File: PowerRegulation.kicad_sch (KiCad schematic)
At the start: 30 parts, among them J11 24V_Lockout_Key_Switch, J12 XT60-M, K1 G5LE-1, Q7 BSS138, U6 XC6206P332MR, U7 TPS5430DDA, U8 TPS5430DDA

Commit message: Fix silk screening
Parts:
- J11, J12, K1: now left out of the parts list
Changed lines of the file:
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@@
 	(title_block
 		(title "Power Distribution")
-		(rev "0.1.0")
+		(rev "1.0.0")
 		(company "Queen's Rocket Engineering Team")
 	)
@@
 		(unit 1)
 		(exclude_from_sim no)
-		(in_bom yes)
+		(in_bom no)
 		(on_board yes)
 		(dnp no)
@@
 		(unit 1)
 		(exclude_from_sim no)
-		(in_bom yes)
+		(in_bom no)
 		(on_board yes)
 		(dnp no)
@@
 		(unit 1)
 		(exclude_from_sim no)
-		(in_bom yes)
+		(in_bom no)
 		(on_board yes)
 		(dnp no)

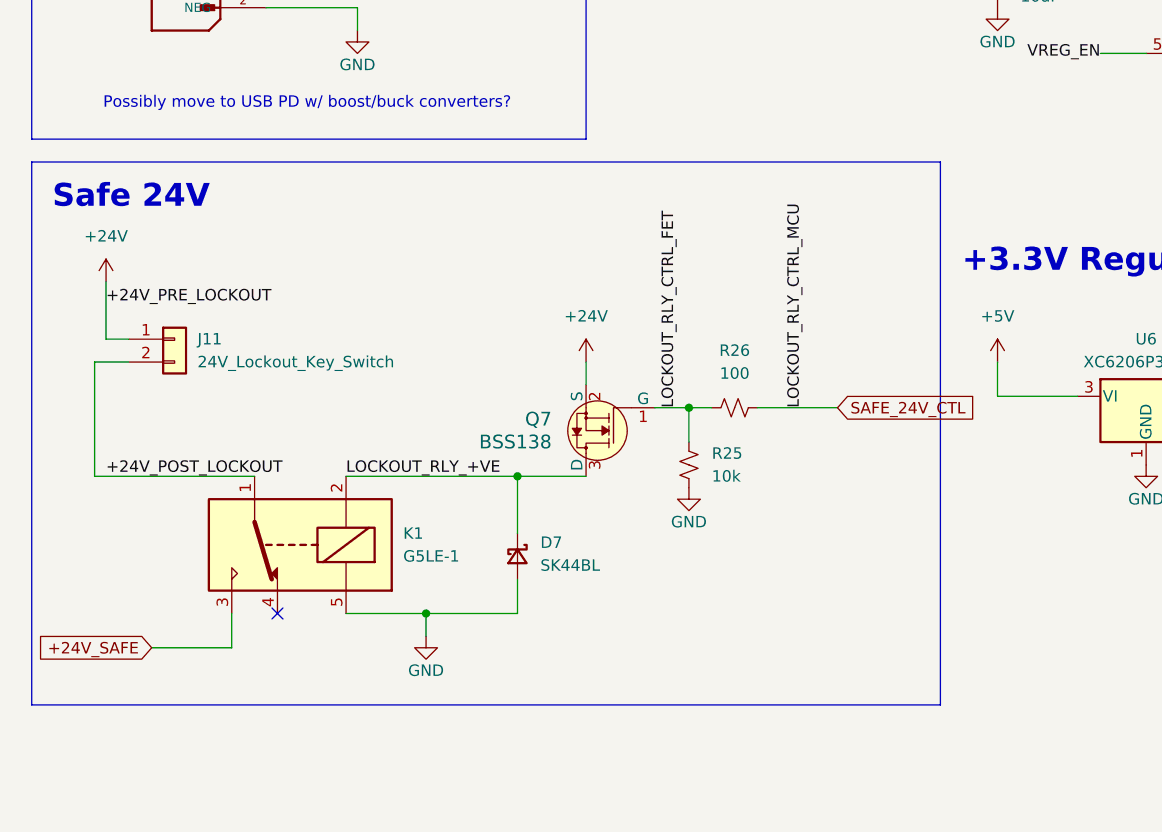
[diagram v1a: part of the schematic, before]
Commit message: Switch relay driving FETs to low side. Relays changed to SPST instead of SPDT
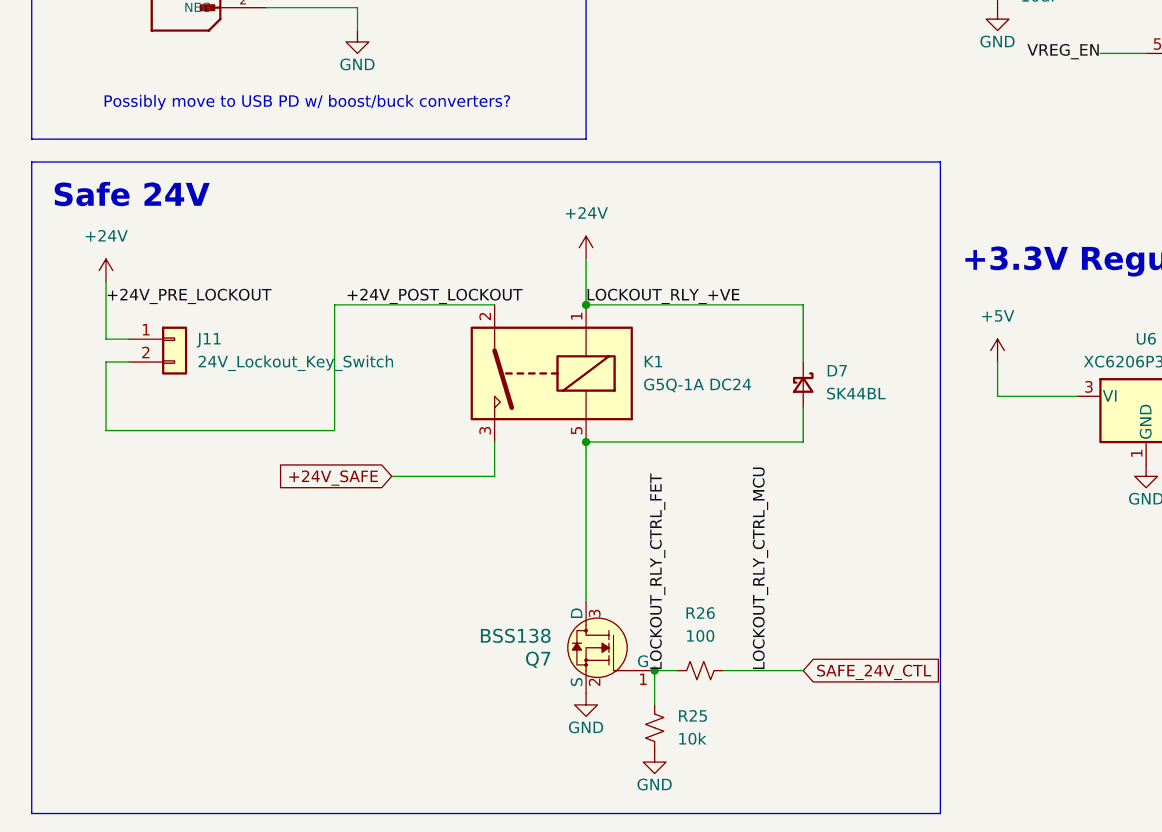
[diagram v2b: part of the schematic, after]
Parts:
- removed K1: G5LE-1, Relay_THT:Relay_SPDT_Omron-G5LE-1, symbol Relay:G5LE-1
- added K1: G5Q-1A DC24, Relay_THT:Relay_SPST_Omron-G5Q-1A, symbol Relay:G5Q-1A
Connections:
- net +24V: now also D7.1 (K), K1.1; no longer Q7.2 (S)
- net +24V_POST_LOCKOUT: now also K1.2
- net +24V_SAFE: now also K1.3
- net GND: now also Q7.2 (S); no longer D7.2 (A)
- net LOCKOUT_RLY_+VE: no longer names the net of Q7.3 (D)
- net LOCKOUT_RLY_+VE: now also D7.2 (A), K1.5; no longer D7.1 (K)
- no-connect marks 2 -> 1
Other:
- moved on the sheet: D7, Q7, R25, R26

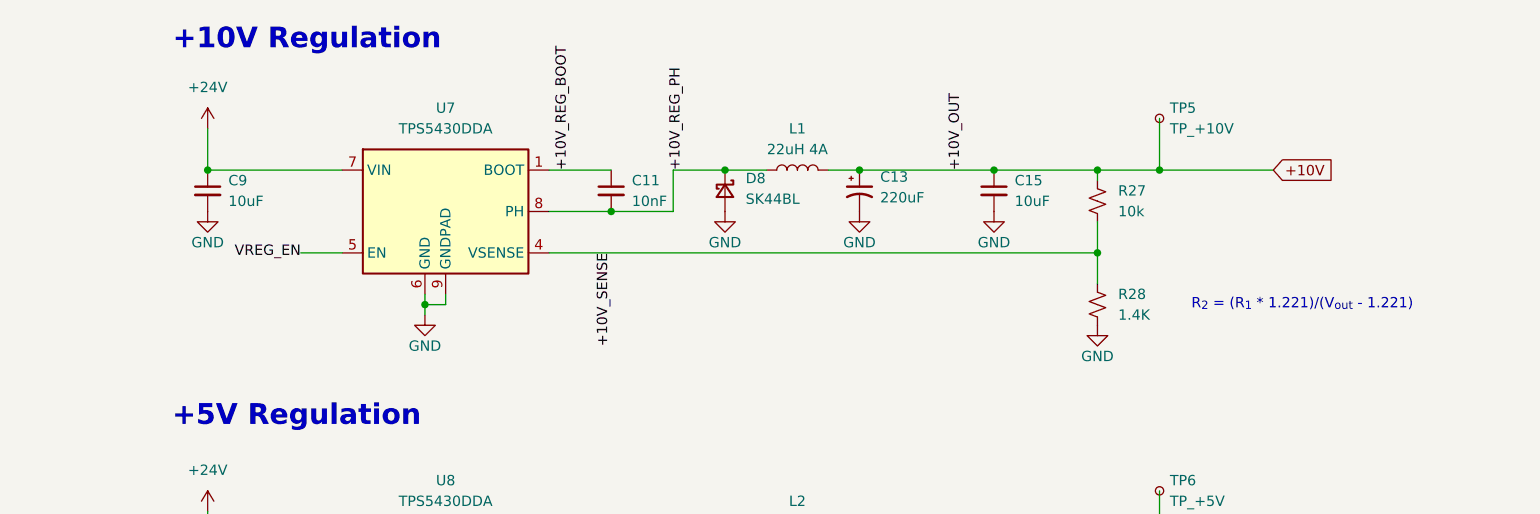
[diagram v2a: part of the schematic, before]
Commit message: Update thrust LC to take +5V. Remove +10V rail
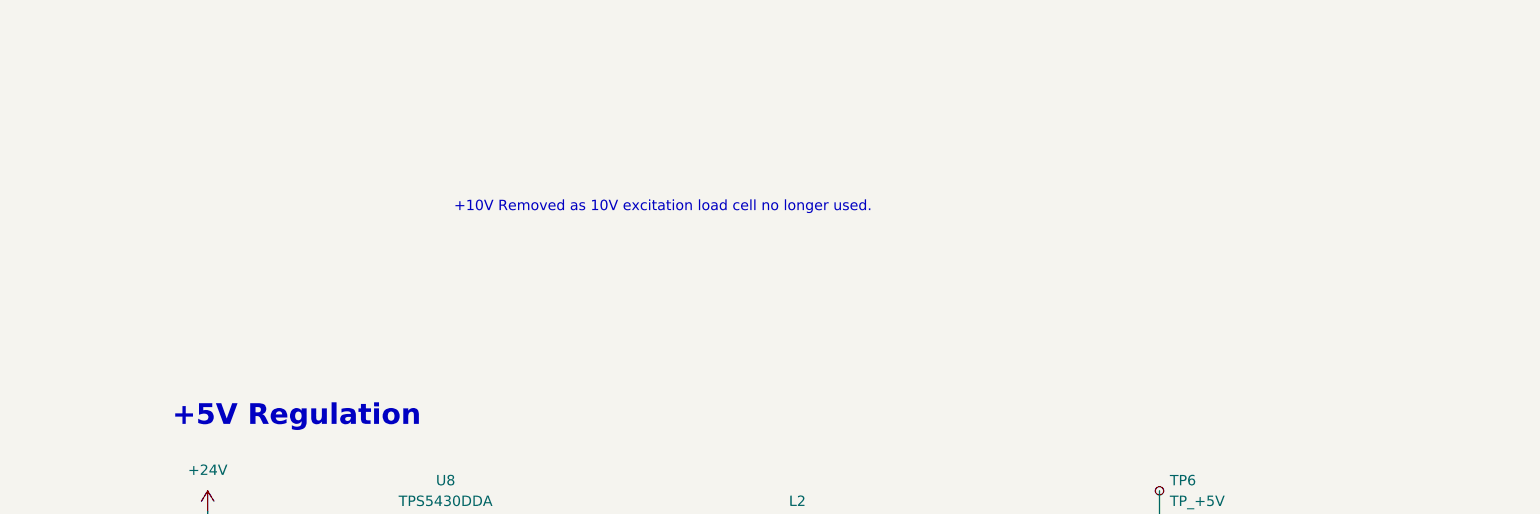
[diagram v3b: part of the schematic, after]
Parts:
- removed C11: 10nF, Capacitor_SMD:C_0402_1005Metric, symbol Device:C_Small
- removed C13: 220uF, Capacitor_SMD:CP_Elec_8x10.5, symbol Device:C_Polarized_Small_US
- removed C15, C9: 10uF, Capacitor_SMD:C_1206_3216Metric, symbol Device:C_Small
- removed D8: SK44BL, Diode_SMD:D_SMB, symbol Device:D_Schottky_Small
- removed L1: 22uH 4A, Inductor_SMD:L_12.5x12.5mm_SXNSMDRS1275, symbol Device:L
- removed R27: 10k, Resistor_SMD:R_0402_1005Metric, symbol Device:R_Small_US
- removed R28: 1.4K, Resistor_SMD:R_0402_1005Metric, symbol Device:R_Small_US
- removed TP5: TP_+10V, TestPoint:TestPoint_Pad_D1.0mm, symbol Connector:TestPoint_Small
- removed U7: TPS5430DDA, Package_SO:TI_SO-PowerPAD-8_ThermalVias, symbol Regulator_Switching:TPS5430DDA
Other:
- note added: "+10V Removed as 10V excitation load cell no longer used."
- note removed: "+10V Regulation"

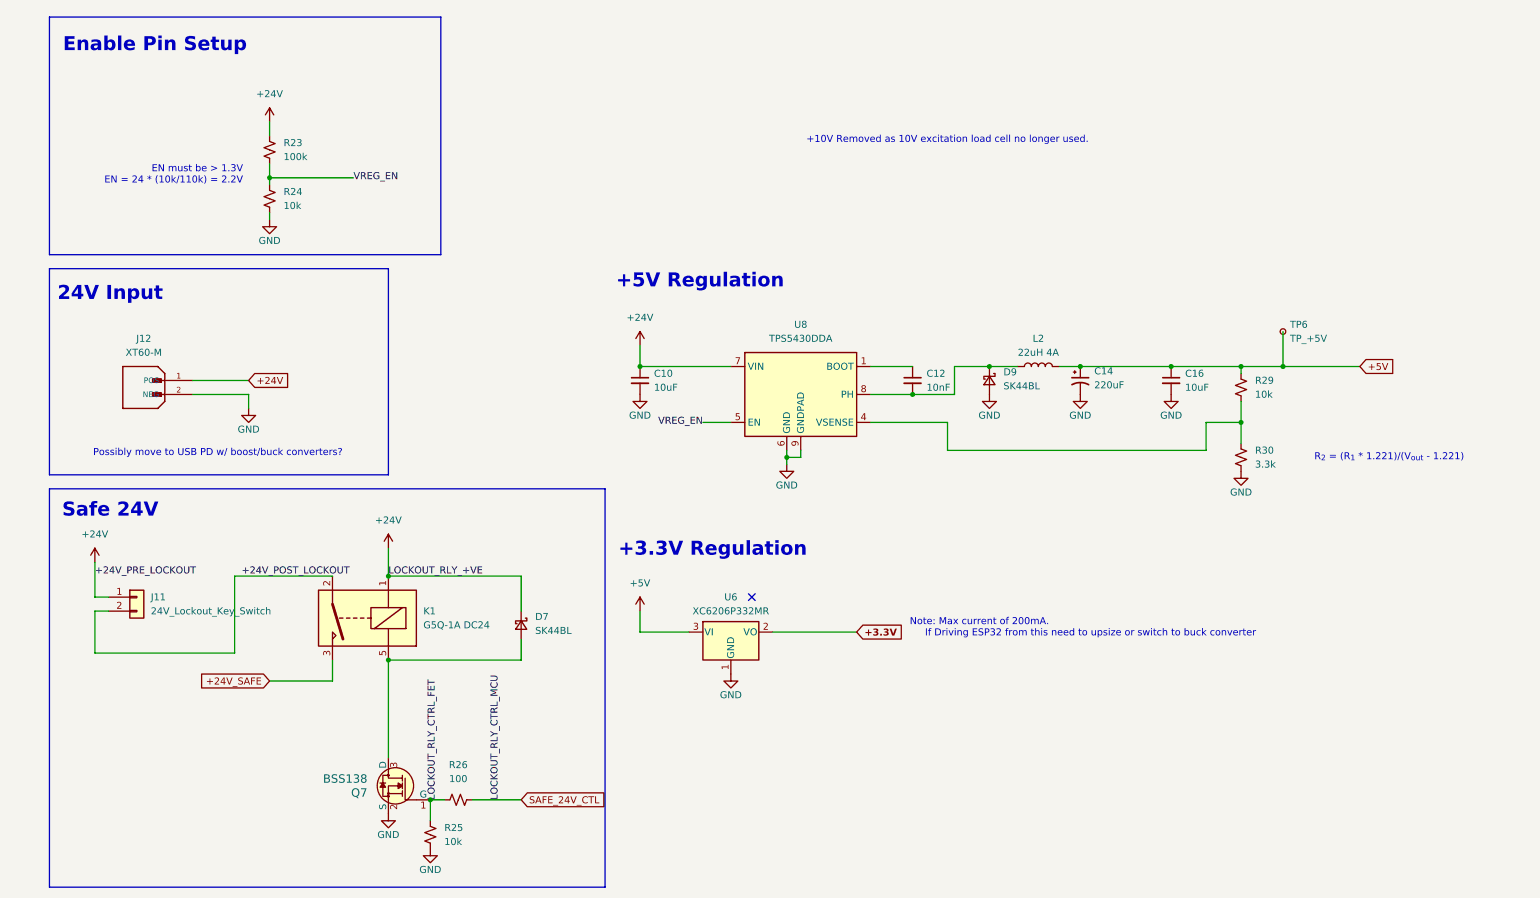
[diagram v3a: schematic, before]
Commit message: Add indicator LEDs and digital +24VSafe detection line
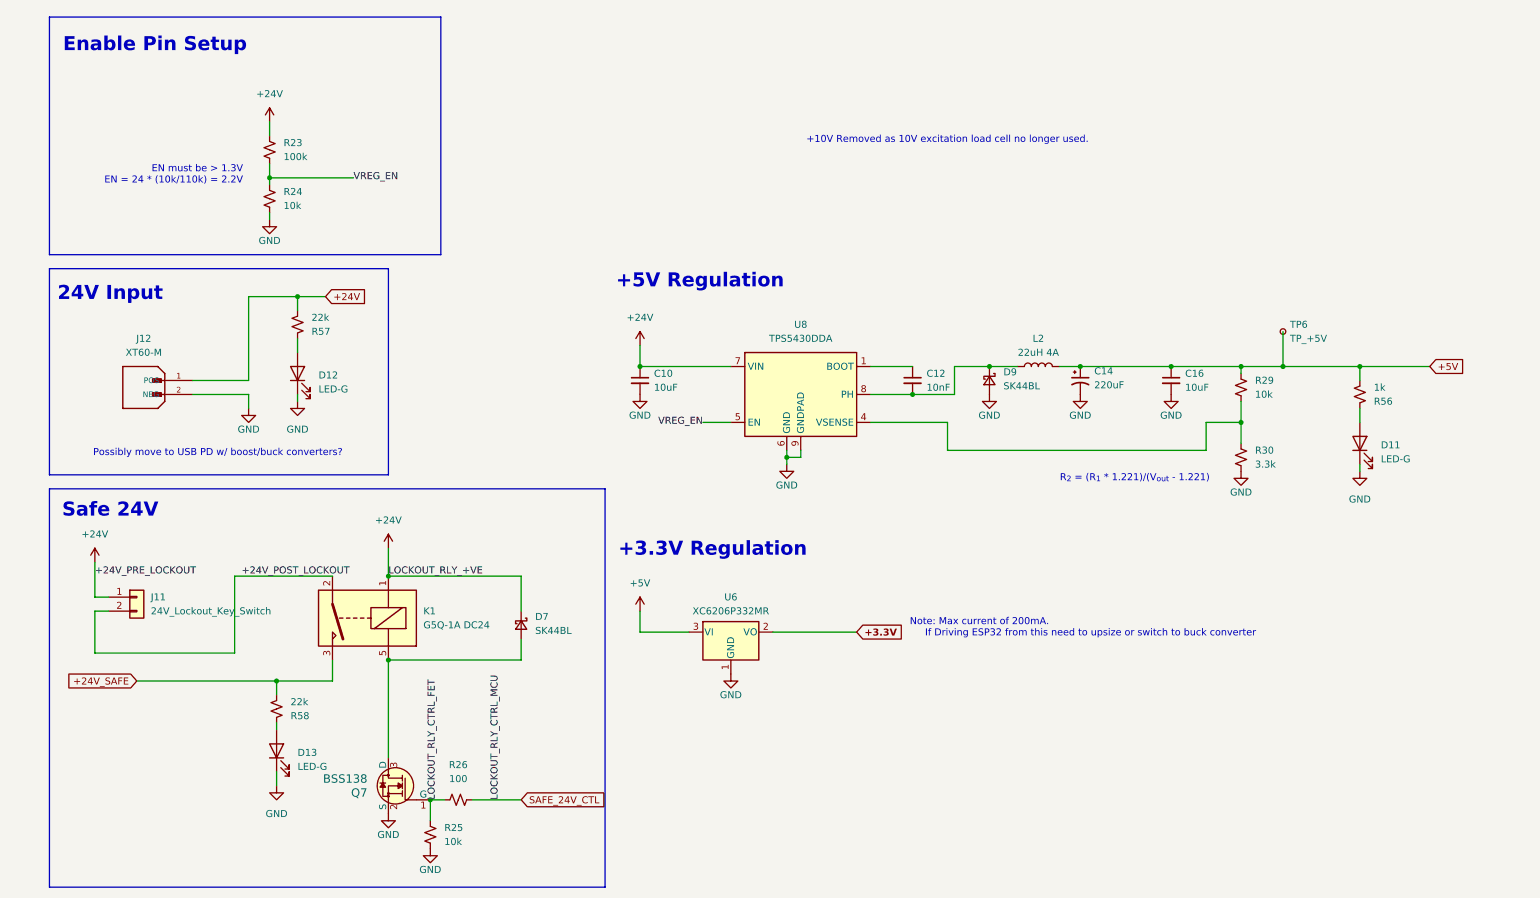
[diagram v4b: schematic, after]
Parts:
- added D11, D12, D13: LED-G, LED_SMD:LED_0805_2012Metric, symbol Device:LED
- added R56: 1k, Resistor_SMD:R_0402_1005Metric, symbol Device:R_Small_US
- added R57, R58: 22k, Resistor_SMD:R_0402_1005Metric, symbol Device:R_Small_US
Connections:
- net +24V: now also R57.2
- net +24V_SAFE: now also R58.2
- net +5V: now also R56.2
- net GND: now also D11.1 (K), D12.1 (K), D13.1 (K)
- new net: D11.2 (A), R56.1
- new net: D12.2 (A), R57.1
- new net: D13.2 (A), R58.1
- no-connect marks 1 -> 0

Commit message: Completed necessary ESP32 wiring + new 3.3V LDO. GPIO pins not yet connected
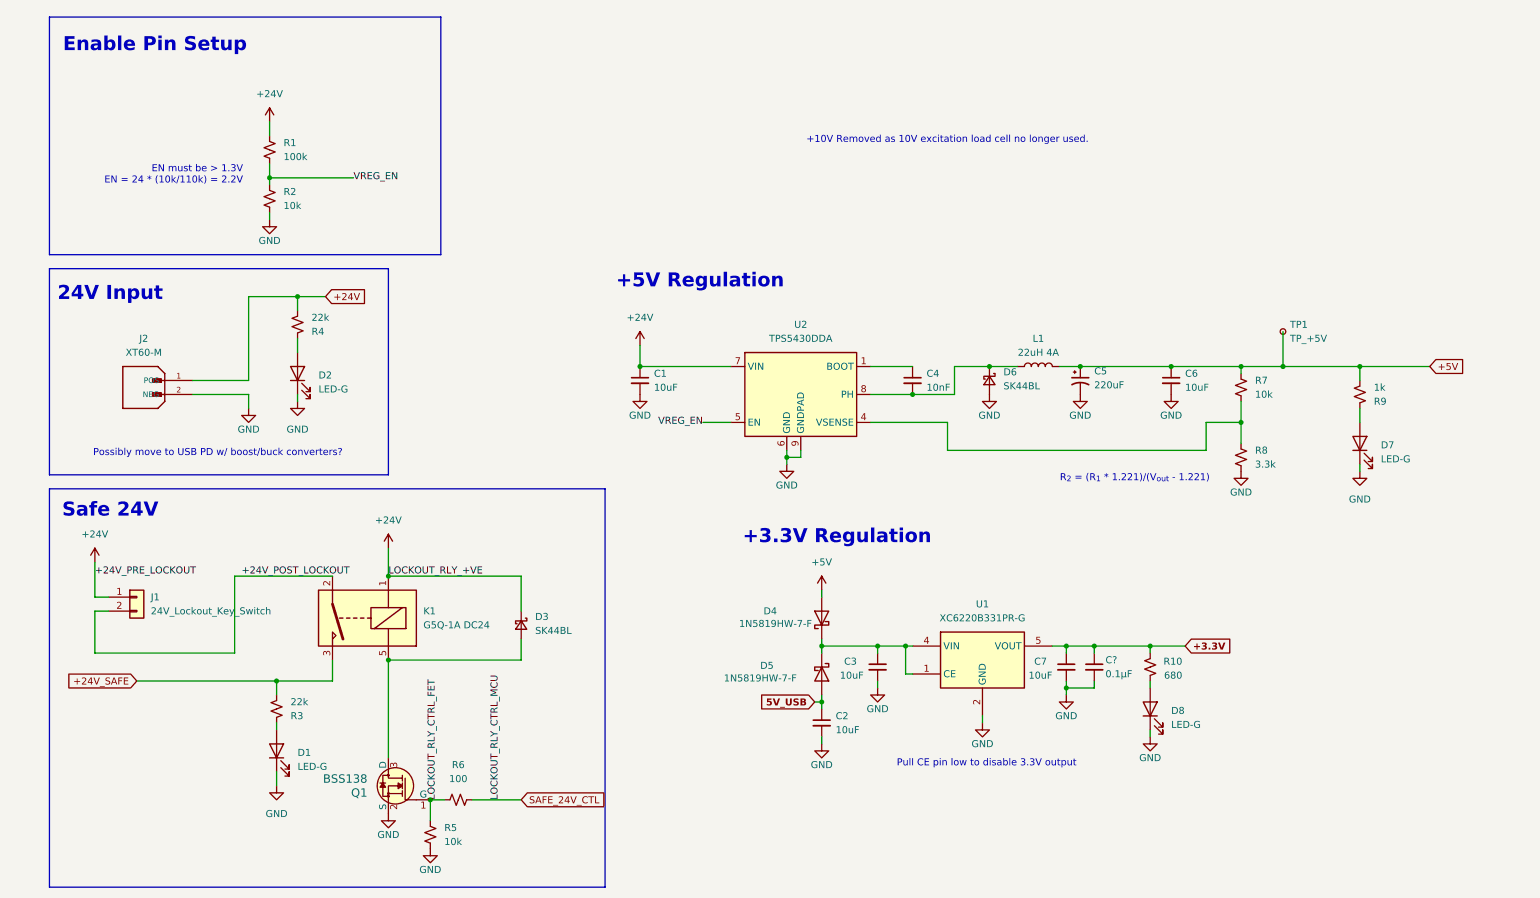
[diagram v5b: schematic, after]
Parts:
- removed U6: XC6206P332MR, Package_TO_SOT_SMD:SOT-23-3, symbol Regulator_Linear:XC6206PxxxMR
- added C2, C3, C7: 10uF, Capacitor_SMD:C_1206_3216Metric, symbol Device:C_Small
- added C?: 0.1μF, Capacitor_SMD:C_0402_1005Metric, symbol Device:C_Small
- added D4, D5: 1N5819HW-7-F, Diode_SMD:D_SOD-123, symbol Diode:MBR0540
- added D8: LED-G, LED_SMD:LED_0805_2012Metric, symbol Device:LED
- added R10: 680, Resistor_SMD:R_0402_1005Metric, symbol Device:R_Small_US
- added U1: XC6220B331PR-G, Package_TO_SOT_SMD:SOT-89-5, symbol Regulator_Linear:XC6220B331MR
- renumbered C10 to C1, C12 to C4, C14 to C5, C16 to C6, D13 to D1, D12 to D2, D7 to D3, D9 to D6, D11 to D7, J11 to J1, J12 to J2, L2 to L1, Q7 to Q1, R23 to R1, R24 to R2, R58 to R3, R57 to R4, R25 to R5, R26 to R6, R29 to R7, R30 to R8, R56 to R9, TP6 to TP1, U8 to U2
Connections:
- net +3.3V: now also C7.1, C?.1, R10.2, U1.5 (VOUT)
- net +5V: now also D4.2 (A)
- net GND: now also C2.2, C3.2, C7.2, C?.2, D8.1 (K), U1.2 (GND)
- new net: D8.2 (A), R10.1
- new net: C3.1, D4.1 (K), D5.1 (K), U1.1 (CE), U1.4 (NC)
- new net 5V_USB: C2.1, D5.2 (A)
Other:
- note added: "Pull CE pin low to disable 3.3V output"
- note removed: "Note: Max current of 200mA. If Driving ESP32 from this need to upsize or switch to buck converter"
